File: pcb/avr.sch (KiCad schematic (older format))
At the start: 30 parts, among them IC2 ATMEGA168-P, P10 CONNECTOR, P11 CONNECTOR, P12 CONNECTOR, P13 CONNECTOR, P14 CONNECTOR, P15 CONNECTOR, P16 CONNECTOR, P17 CONNECTOR, P18 CONNECTOR, P19 CONNECTOR, P20 CONNECTOR, P21 CONNECTOR, P22 CONNECTOR, P23 CONNECTOR, P24 CONNECTOR, P25 CONN_01X03, P4 CONNECTOR, P5 CONNECTOR, P6 CONNECTOR, P7 CONNECTOR, P8 CONNECTOR, P9 CONNECTOR, x2 xtal_osc

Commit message: changed LED and boost converters Diode footprints. renumbered components
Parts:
- renumbered C13 to C201, C14 to C202, C10 to C203, C11 to C204, C12 to C205, IC2 to IC201, P4 to P201, P5 to P202, P6 to P203, P7 to P204, P8 to P205, P9 to P206, P10 to P207, P11 to P208, P12 to P209, P13 to P210, P14 to P211, P15 to P212, P16 to P213, P17 to P214, P18 to P215, P19 to P216, P20 to P217, P21 to P218, P22 to P219, P23 to P220, P24 to P221, P25 to P222, R5 to R201, x2 to x201
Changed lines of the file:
@@
 Connection ~ 4750 2900
 $Comp
-L xtal_osc x2
+L xtal_osc x201
 U 1 1 58B9F491
 P 8900 4000
-F 0 "x2" H 8750 4250 60  0000 C CNN
+F 0 "x201" H 8750 4250 60  0000 C CNN
 F 1 "xtal_osc" H 8900 4150 60  0000 C CNN
 F 2 "netl:SM_3225" H 8900 4050 60  0001 C CNN
@@
 $EndComp
 $Comp
-L GND #PWR015
+L GND #PWR202
 U 1 1 58B9F648
 P 4800 4950
-F 0 "#PWR015" H 4800 4700 50  0001 C CNN
+F 0 "#PWR202" H 4800 4700 50  0001 C CNN
 F 1 "GND" H 4800 4800 50  0000 C CNN
 F 2 "" H 4800 4950 50  0000 C CNN
@@
 Connection ~ 4800 4900
 $Comp
-L GND #PWR016
+L GND #PWR204
 U 1 1 58B9F675
 P 8900 4300
-F 0 "#PWR016" H 8900 4050 50  0001 C CNN
+F 0 "#PWR204" H 8900 4050 50  0001 C CNN
 F 1 "GND" H 8900 4150 50  0000 C CNN
 F 2 "" H 8900 4300 50  0000 C CNN
@@
 Connection ~ 8900 4300
 $Comp
-L C C10
+L C C203
 U 1 1 58B9F6BE
 P 8450 4150
-F 0 "C10" H 8475 4250 50  0000 L CNN
+F 0 "C203" H 8475 4250 50  0000 L CNN
 F 1 "C" H 8475 4050 50  0000 L CNN
 F 2 "netl:SMD_0603" H 8488 4000 50  0001 C CNN
@@
 $EndComp
 $Comp
-L C C12
+L C C205
 U 1 1 58B9F6FA
 P 9350 4150
-F 0 "C12" H 9375 4250 50  0000 L CNN
+F 0 "C205" H 9375 4250 50  0000 L CNN
 F 1 "C" H 9375 4050 50  0000 L CNN
 F 2 "netl:SMD_0603" H 9388 4000 50  0001 C CNN
@@
 $EndComp
 $Comp
-L GND #PWR017
+L GND #PWR203
 U 1 1 58B9F75B
 P 8450 4300
-F 0 "#PWR017" H 8450 4050 50  0001 C CNN
+F 0 "#PWR203" H 8450 4050 50  0001 C CNN
 F 1 "GND" H 8450 4150 50  0000 C CNN
 F 2 "" H 8450 4300 50  0000 C CNN
@@
 $EndComp
 $Comp
-L GND #PWR018
+L GND #PWR205
 U 1 1 58B9F772
 P 9350 4300
-F 0 "#PWR018" H 9350 4050 50  0001 C CNN
+F 0 "#PWR205" H 9350 4050 50  0001 C CNN
 F 1 "GND" H 9350 4150 50  0000 C CNN
 F 2 "" H 9350 4300 50  0000 C CNN
@@
 Connection ~ 9350 4000
 $Comp
-L R R5
+L R R201
 U 1 1 58B9FA6E
 P 9050 2900
-F 0 "R5" V 9130 2900 50  0000 C CNN
+F 0 "R201" V 9130 2900 50  0000 C CNN
 F 1 "R" V 9050 2900 50  0000 C CNN
 F 2 "netl:SMD_0603" V 8980 2900 50  0001 C CNN
@@
 ~DTR
 $Comp
-L C C11
+L C C204
 U 1 1 58B9FE16
 P 8900 3050
-F 0 "C11" H 8925 3150 50  0000 L CNN
+F 0 "C204" H 8925 3150 50  0000 L CNN
 F 1 "C" H 8925 2950 50  0000 L CNN
 F 2 "netl:SMD_0603" H 8938 2900 50  0001 C CNN
@@
 TX
 $Comp
-L C C13
+L C C201
 U 1 1 58BA2D1E
 P 4150 3000
-F 0 "C13" H 4175 3100 50  0000 L CNN
+F 0 "C201" H 4175 3100 50  0000 L CNN
 F 1 "C" H 4175 2900 50  0000 L CNN
 F 2 "netl:SMD_0603" H 4188 2850 50  0001 C CNN
@@
 $EndComp
 $Comp
-L C C14
+L C C202
 U 1 1 58BA4005
 P 4450 3000
-F 0 "C14" H 4475 3100 50  0000 L CNN
+F 0 "C202" H 4475 3100 50  0000 L CNN
 F 1 "C" H 4475 2900 50  0000 L CNN
 F 2 "netl:SMD_0603" H 4488 2850 50  0001 C CNN
@@
 $EndComp
 $Comp
-L GND #PWR019
+L GND #PWR201
 U 1 1 58BA4083
 P 4300 3250
-F 0 "#PWR019" H 4300 3000 50  0001 C CNN
+F 0 "#PWR201" H 4300 3000 50  0001 C CNN
 F 1 "GND" H 4300 3100 50  0000 C CNN
 F 2 "" H 4300 3250 50  0000 C CNN
@@
 Connection ~ 4300 2850
 $Comp
-L CONNECTOR P17
+L CONNECTOR P214
 U 1 1 58BA814A
 P 6850 4200
-F 0 "P17" H 7300 4200 70  0000 C CNN
+F 0 "P214" H 7300 4200 70  0000 C CNN
 F 1 "CONNECTOR" H 7150 4450 70  0001 C CNN
 F 2 "netl:1Pin_small" H 6850 4200 60  0001 C CNN
@@
 $EndComp
 $Comp
-L CONNECTOR P18
+L CONNECTOR P215
 U 1 1 58BA8D9B
 P 6850 4300
-F 0 "P18" H 7300 4300 70  0000 C CNN
+F 0 "P215" H 7300 4300 70  0000 C CNN
 F 1 "CONNECTOR" H 7150 4550 70  0001 C CNN
 F 2 "netl:1Pin_small" H 6850 4300 60  0001 C CNN
@@
 $EndComp
 $Comp
-L CONNECTOR P19
+L CONNECTOR P216
 U 1 1 58BA8DC9
 P 6850 4400
-F 0 "P19" H 7300 4400 70  0000 C CNN
+F 0 "P216" H 7300 4400 70  0000 C CNN
 F 1 "CONNECTOR" H 7150 4650 70  0001 C CNN
 F 2 "netl:1Pin_small" H 6850 4400 60  0001 C CNN
@@
 $EndComp
 $Comp
-L CONNECTOR P20
+L CONNECTOR P217
 U 1 1 58BA8DFA
 P 6850 4500
-F 0 "P20" H 7300 4500 70  0000 C CNN
+F 0 "P217" H 7300 4500 70  0000 C CNN
 F 1 "CONNECTOR" H 7150 4750 70  0001 C CNN
 F 2 "netl:1Pin_small" H 6850 4500 60  0001 C CNN
@@
 $EndComp
 $Comp
-L CONNECTOR P21
+L CONNECTOR P218
 U 1 1 58BA8E32
 P 6850 4600
-F 0 "P21" H 7300 4600 70  0000 C CNN
+F 0 "P218" H 7300 4600 70  0000 C CNN
 F 1 "CONNECTOR" H 7150 4850 70  0001 C CNN
 F 2 "netl:1Pin_small" H 6850 4600 60  0001 C CNN
@@
 $EndComp
 $Comp
-L CONNECTOR P22
+L CONNECTOR P219
 U 1 1 58BA8E6D
 P 6850 4700
-F 0 "P22" H 7300 4700 70  0000 C CNN
+F 0 "P219" H 7300 4700 70  0000 C CNN
 F 1 "CONNECTOR" H 7150 4950 70  0001 C CNN
 F 2 "netl:1Pin_small" H 6850 4700 60  0001 C CNN
@@
 $EndComp
 $Comp
-L CONNECTOR P23
+L CONNECTOR P220
 U 1 1 58BA8ED1
 P 6850 4800
-F 0 "P23" H 7300 4800 70  0000 C CNN
+F 0 "P220" H 7300 4800 70  0000 C CNN
 F 1 "CONNECTOR" H 7150 5050 70  0001 C CNN
 F 2 "netl:1Pin_small" H 6850 4800 60  0001 C CNN
@@
 $EndComp
 $Comp
-L CONNECTOR P24
+L CONNECTOR P221
 U 1 1 58BA8F12
 P 6850 4900
-F 0 "P24" H 7300 4900 70  0000 C CNN
+F 0 "P221" H 7300 4900 70  0000 C CNN
 F 1 "CONNECTOR" H 7150 5150 70  0001 C CNN
 F 2 "netl:1Pin_small" H 6850 4900 60  0001 C CNN
@@
 	6700 3450 6850 3450
 $Comp
-L CONNECTOR P10
+L CONNECTOR P207
 U 1 1 58BA94D6
 P 6850 3450
-F 0 "P10" H 7300 3450 70  0000 C CNN
+F 0 "P207" H 7300 3450 70  0000 C CNN
 F 1 "CONNECTOR" H 7150 3700 70  0001 C CNN
 F 2 "netl:1Pin_small" H 6850 3450 60  0001 C CNN
@@
 $EndComp
 $Comp
-L CONNECTOR P11
+L CONNECTOR P208
 U 1 1 58BA94DC
 P 6850 3550
-F 0 "P11" H 7300 3550 70  0000 C CNN
+F 0 "P208" H 7300 3550 70  0000 C CNN
 F 1 "CONNECTOR" H 7150 3800 70  0001 C CNN
 F 2 "netl:1Pin_small" H 6850 3550 60  0001 C CNN
@@
 $EndComp
 $Comp
-L CONNECTOR P12
+L CONNECTOR P209
 U 1 1 58BA94E2
 P 6850 3650
-F 0 "P12" H 7300 3650 70  0000 C CNN
+F 0 "P209" H 7300 3650 70  0000 C CNN
 F 1 "CONNECTOR" H 7150 3900 70  0001 C CNN
 F 2 "netl:1Pin_small" H 6850 3650 60  0001 C CNN
@@
 $EndComp
 $Comp
-L CONNECTOR P13
+L CONNECTOR P210
 U 1 1 58BA94E8
 P 6850 3750
-F 0 "P13" H 7300 3750 70  0000 C CNN
+F 0 "P210" H 7300 3750 70  0000 C CNN
 F 1 "CONNECTOR" H 7150 4000 70  0001 C CNN
 F 2 "netl:1Pin_small" H 6850 3750 60  0001 C CNN
@@
 $EndComp
 $Comp
-L CONNECTOR P14
+L CONNECTOR P211
 U 1 1 58BA94EE
 P 6850 3850
-F 0 "P14" H 7300 3850 70  0000 C CNN
+F 0 "P211" H 7300 3850 70  0000 C CNN
 F 1 "CONNECTOR" H 7150 4100 70  0001 C CNN
 F 2 "netl:1Pin_small" H 6850 3850 60  0001 C CNN
@@
 $EndComp
 $Comp
-L CONNECTOR P15
+L CONNECTOR P212
 U 1 1 58BA94F4
 P 6850 3950
-F 0 "P15" H 7300 3950 70  0000 C CNN
+F 0 "P212" H 7300 3950 70  0000 C CNN
 F 1 "CONNECTOR" H 7150 4200 70  0001 C CNN
 F 2 "netl:1Pin_small" H 6850 3950 60  0001 C CNN
@@
 $EndComp
 $Comp
-L CONNECTOR P16
+L CONNECTOR P213
 U 1 1 58BA94FA
 P 6850 4050
-F 0 "P16" H 7300 4050 70  0000 C CNN
+F 0 "P213" H 7300 4050 70  0000 C CNN
 F 1 "CONNECTOR" H 7150 4300 70  0001 C CNN
 F 2 "netl:1Pin_small" H 6850 4050 60  0001 C CNN
@@
 	6850 4050 6700 4050
 $Comp
-L ATMEGA168-P IC2
+L ATMEGA168-P IC201
 U 1 1 58B9E598
 P 5800 3750
-F 0 "IC2" H 4950 5050 50  0000 L BNN
+F 0 "IC201" H 4950 5050 50  0000 L BNN
 F 1 "ATMEGA168-P" H 6150 2400 50  0000 L BNN
 F 2 "Housings_QFP:TQFP-32_7x7mm_Pitch0.8mm" H 5800 2350 50  0000 C CIN
@@
 $EndComp
 Wire Wire Line
-	6700 4200 6850 4200
-Wire Wire Line
-	6850 4300 6700 4300
-Wire Wire Line
-	6700 4300 6700 4250
-Wire Wire Line
-	6700 4150 6700 4200
-Wire Wire Line
 	6700 2600 6850 2600
 $Comp
-L CONNECTOR P4
+L CONNECTOR P201
 U 1 1 58BA9F9A
 P 6850 2600
-F 0 "P4" H 7300 2600 70  0000 C CNN
+F 0 "P201" H 7300 2600 70  0000 C CNN
 F 1 "CONNECTOR" H 7150 2850 70  0001 C CNN
 F 2 "netl:1Pin_small" H 6850 2600 60  0001 C CNN
@@
 $EndComp
 $Comp
-L CONNECTOR P5
+L CONNECTOR P202
 U 1 1 58BA9FA0
 P 6850 2700
-F 0 "P5" H 7300 2700 70  0000 C CNN
+F 0 "P202" H 7300 2700 70  0000 C CNN
 F 1 "CONNECTOR" H 7150 2950 70  0001 C CNN
 F 2 "netl:1Pin_small" H 6850 2700 60  0001 C CNN
@@
 $EndComp
 $Comp
-L CONNECTOR P6
+L CONNECTOR P203
 U 1 1 58BA9FA6
 P 6850 2800
-F 0 "P6" H 7300 2800 70  0000 C CNN
+F 0 "P203" H 7300 2800 70  0000 C CNN
 F 1 "CONNECTOR" H 7150 3050 70  0001 C CNN
 F 2 "netl:1Pin_small" H 6850 2800 60  0001 C CNN
@@
 $EndComp
 $Comp
-L CONNECTOR P7
+L CONNECTOR P204
 U 1 1 58BA9FAC
 P 6850 2900
-F 0 "P7" H 7300 2900 70  0000 C CNN
+F 0 "P204" H 7300 2900 70  0000 C CNN
 F 1 "CONNECTOR" H 7150 3150 70  0001 C CNN
 F 2 "netl:1Pin_small" H 6850 2900 60  0001 C CNN
@@
 $EndComp
 $Comp
-L CONNECTOR P8
+L CONNECTOR P205
 U 1 1 58BA9FB2
 P 6850 3000
-F 0 "P8" H 7300 3000 70  0000 C CNN
+F 0 "P205" H 7300 3000 70  0000 C CNN
 F 1 "CONNECTOR" H 7150 3250 70  0001 C CNN
 F 2 "netl:1Pin_small" H 6850 3000 60  0001 C CNN
@@
 $EndComp
 $Comp
-L CONNECTOR P9
+L CONNECTOR P206
 U 1 1 58BA9FB8
 P 6850 3100
-F 0 "P9" H 7300 3100 70  0000 C CNN
+F 0 "P206" H 7300 3100 70  0000 C CNN
 F 1 "CONNECTOR" H 7150 3350 70  0001 C CNN
 F 2 "netl:1Pin_small" H 6850 3100 60  0001 C CNN
@@
 	6700 3100 6850 3100
 $Comp
-L CONN_01X03 P25
+L CONN_01X03 P222
 U 1 1 58BAB28B
 P 10600 4200
-F 0 "P25" H 10600 4400 50  0000 C CNN
+F 0 "P222" H 10600 4400 50  0000 C CNN
 F 1 "CONN_01X03" V 10700 4200 50  0000 C CNN
 F 2 "netl:SM_3_WIRE" H 10600 4200 50  0000 C CNN
@@
 $EndComp
 $Comp
-L GND #PWR020
+L GND #PWR206
 U 1 1 58BAB3DE
 P 10350 4350
-F 0 "#PWR020" H 10350 4100 50  0001 C CNN
+F 0 "#PWR206" H 10350 4100 50  0001 C CNN
 F 1 "GND" H 10350 4200 50  0000 C CNN
 F 2 "" H 10350 4350 50  0000 C CNN
@@
 Wire Wire Line
 	10400 4100 10350 4100
+Wire Wire Line
+	6700 4200 6850 4200
+Wire Wire Line
+	6700 4150 6700 4200
+Wire Wire Line
+	6700 4300 6850 4300
+Wire Wire Line
+	6700 4250 6700 4300
 $EndSCHEMATC

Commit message: changed mcu to the correct one. redid layout
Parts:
- removed IC201: ATMEGA168-P, Housings_QFP:TQFP-32_7x7mm_Pitch0.8mm, symbol ATMEGA168-P
- added IC201: ATMEGA328P-M, MLF/QFN32, symbol ATMEGA328P-M
- added P223, P224: CONNECTOR, netl:1Pin_small, symbol CONNECTOR
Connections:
- wire segments 43 -> 44
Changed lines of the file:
@@
 	4650 4900 4800 4900
 Wire Wire Line
-	4800 4800 4800 4950
+	4800 4700 4800 4950
 Text HLabel 4350 2600 0    60   Input ~ 0
 VCC
@@
 $EndComp
 $Comp
-L GND #PWR202
+L GND #PWR08
 U 1 1 58B9F648
 P 4800 4950
-F 0 "#PWR202" H 4800 4700 50  0001 C CNN
+F 0 "#PWR08" H 4800 4700 50  0001 C CNN
 F 1 "GND" H 4800 4800 50  0000 C CNN
 F 2 "" H 4800 4950 50  0000 C CNN
@@
 Connection ~ 4800 4900
 $Comp
-L GND #PWR204
+L GND #PWR09
 U 1 1 58B9F675
 P 8900 4300
-F 0 "#PWR204" H 8900 4050 50  0001 C CNN
+F 0 "#PWR09" H 8900 4050 50  0001 C CNN
 F 1 "GND" H 8900 4150 50  0000 C CNN
 F 2 "" H 8900 4300 50  0000 C CNN
@@
 $EndComp
 $Comp
-L GND #PWR203
+L GND #PWR010
 U 1 1 58B9F75B
 P 8450 4300
-F 0 "#PWR203" H 8450 4050 50  0001 C CNN
+F 0 "#PWR010" H 8450 4050 50  0001 C CNN
 F 1 "GND" H 8450 4150 50  0000 C CNN
 F 2 "" H 8450 4300 50  0000 C CNN
@@
 $EndComp
 $Comp
-L GND #PWR205
+L GND #PWR011
 U 1 1 58B9F772
 P 9350 4300
-F 0 "#PWR205" H 9350 4050 50  0001 C CNN
+F 0 "#PWR011" H 9350 4050 50  0001 C CNN
 F 1 "GND" H 9350 4150 50  0000 C CNN
 F 2 "" H 9350 4300 50  0000 C CNN
@@
 $EndComp
 $Comp
-L GND #PWR201
+L GND #PWR012
 U 1 1 58BA4083
 P 4300 3250
-F 0 "#PWR201" H 4300 3000 50  0001 C CNN
+F 0 "#PWR012" H 4300 3000 50  0001 C CNN
 F 1 "GND" H 4300 3100 50  0000 C CNN
 F 2 "" H 4300 3250 50  0000 C CNN
@@
 	6850 4050 6700 4050
 $Comp
-L ATMEGA168-P IC201
-U 1 1 58B9E598
-P 5800 3750
-F 0 "IC201" H 4950 5050 50  0000 L BNN
-F 1 "ATMEGA168-P" H 6150 2400 50  0000 L BNN
-F 2 "Housings_QFP:TQFP-32_7x7mm_Pitch0.8mm" H 5800 2350 50  0000 C CIN
-F 3 "" H 5800 3750 50  0000 C CNN
-	1    5800 3750
-	1    0    0    -1
-$EndComp
-Wire Wire Line
-	6700 2600 6850 2600
-$Comp
 L CONNECTOR P201
 U 1 1 58BA9F9A
@@
 $EndComp
 $Comp
-L GND #PWR206
+L GND #PWR013
 U 1 1 58BAB3DE
 P 10350 4350
-F 0 "#PWR206" H 10350 4100 50  0001 C CNN
+F 0 "#PWR013" H 10350 4100 50  0001 C CNN
 F 1 "GND" H 10350 4200 50  0000 C CNN
 F 2 "" H 10350 4350 50  0000 C CNN
@@
 Wire Wire Line
 	10350 4300 10350 4350
-Text Label 6700 2600 0    60   ~ 0
+Text Label 6700 4400 0    60   ~ 0
 LED_SRIP
 Text Label 10350 4200 2    60   ~ 0
@@
 Wire Wire Line
 	6700 4250 6700 4300
+$Comp
+L ATMEGA328P-M IC201
+U 1 1 590DDCB6
+P 5700 3700
+F 0 "IC201" H 4950 4950 50  0000 L BNN
+F 1 "ATMEGA328P-M" H 6100 2300 50  0000 L BNN
+F 2 "MLF/QFN32" H 5700 3700 50  0000 C CIN
+F 3 "" H 5700 3700 50  0000 C CNN
+	1    5700 3700
+	1    0    0    -1
+$EndComp
+Wire Wire Line
+	4800 2700 4750 2700
+Connection ~ 4750 2700
+Connection ~ 4800 4800
+$Comp
+L CONNECTOR P223
+U 1 1 590DE73E
+P 4800 3950
+F 0 "P223" H 5250 3950 70  0000 C CNN
+F 1 "CONNECTOR" H 5100 4200 70  0001 C CNN
+F 2 "netl:1Pin_small" H 4800 3950 60  0001 C CNN
+F 3 "" H 4800 3950 60  0000 C CNN
+	1    4800 3950
+	-1   0    0    1
+$EndComp
+$Comp
+L CONNECTOR P224
+U 1 1 590DEA2E
+P 4800 4050
+F 0 "P224" H 5250 4050 70  0000 C CNN
+F 1 "CONNECTOR" H 5100 4300 70  0001 C CNN
+F 2 "netl:1Pin_small" H 4800 4050 60  0001 C CNN
+F 3 "" H 4800 4050 60  0000 C CNN
+	1    4800 4050
+	-1   0    0    1
+$EndComp
+Wire Wire Line
+	6850 2600 6700 2600
 $EndSCHEMATC

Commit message: updated component values
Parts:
- C201, C202, C204: value C -> 100n
- C203, C205: value C -> 22p
- R201: value R -> 10k
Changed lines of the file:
@@
 P 8450 4150
 F 0 "C203" H 8475 4250 50  0000 L CNN
-F 1 "C" H 8475 4050 50  0000 L CNN
+F 1 "22p" H 8475 4050 50  0000 L CNN
 F 2 "netl:SMD_0603" H 8488 4000 50  0001 C CNN
 F 3 "" H 8450 4150 50  0000 C CNN
@@
 P 9350 4150
 F 0 "C205" H 9375 4250 50  0000 L CNN
-F 1 "C" H 9375 4050 50  0000 L CNN
+F 1 "22p" H 9375 4050 50  0000 L CNN
 F 2 "netl:SMD_0603" H 9388 4000 50  0001 C CNN
 F 3 "" H 9350 4150 50  0000 C CNN
@@
 P 9050 2900
 F 0 "R201" V 9130 2900 50  0000 C CNN
-F 1 "R" V 9050 2900 50  0000 C CNN
+F 1 "10k" V 9050 2900 50  0000 C CNN
 F 2 "netl:SMD_0603" V 8980 2900 50  0001 C CNN
 F 3 "" H 9050 2900 50  0000 C CNN
@@
 P 8900 3050
 F 0 "C204" H 8925 3150 50  0000 L CNN
-F 1 "C" H 8925 2950 50  0000 L CNN
+F 1 "100n" H 8925 2950 50  0000 L CNN
 F 2 "netl:SMD_0603" H 8938 2900 50  0001 C CNN
 F 3 "" H 8900 3050 50  0000 C CNN
@@
 P 4150 3000
 F 0 "C201" H 4175 3100 50  0000 L CNN
-F 1 "C" H 4175 2900 50  0000 L CNN
+F 1 "100n" H 4175 2900 50  0000 L CNN
 F 2 "netl:SMD_0603" H 4188 2850 50  0001 C CNN
 F 3 "" H 4150 3000 50  0000 C CNN
@@
 P 4450 3000
 F 0 "C202" H 4475 3100 50  0000 L CNN
-F 1 "C" H 4475 2900 50  0000 L CNN
+F 1 "100n" H 4475 2900 50  0000 L CNN
 F 2 "netl:SMD_0603" H 4488 2850 50  0001 C CNN
 F 3 "" H 4450 3000 50  0000 C CNN

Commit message: centered battery tab connectors, reworked layout to match it
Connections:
- net LED_SRIP: now also IC201.1 ((PCINT19/OC2B/INT1)PD3), P217.1 (W); no longer IC201.32 ((PCINT18/INT0)PD2), P216.1 (W)
- new net BTN: IC201.32 ((PCINT18/INT0)PD2), P216.1 (W)
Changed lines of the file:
@@
 Wire Wire Line
 	10350 4300 10350 4350
-Text Label 6700 4400 0    60   ~ 0
+Text Label 6700 4500 0    60   ~ 0
 LED_SRIP
 Text Label 10350 4200 2    60   ~ 0
@@
 Wire Wire Line
 	6850 2600 6700 2600
+Text Label 6700 4400 0    60   ~ 0
+BTN
 $EndSCHEMATC

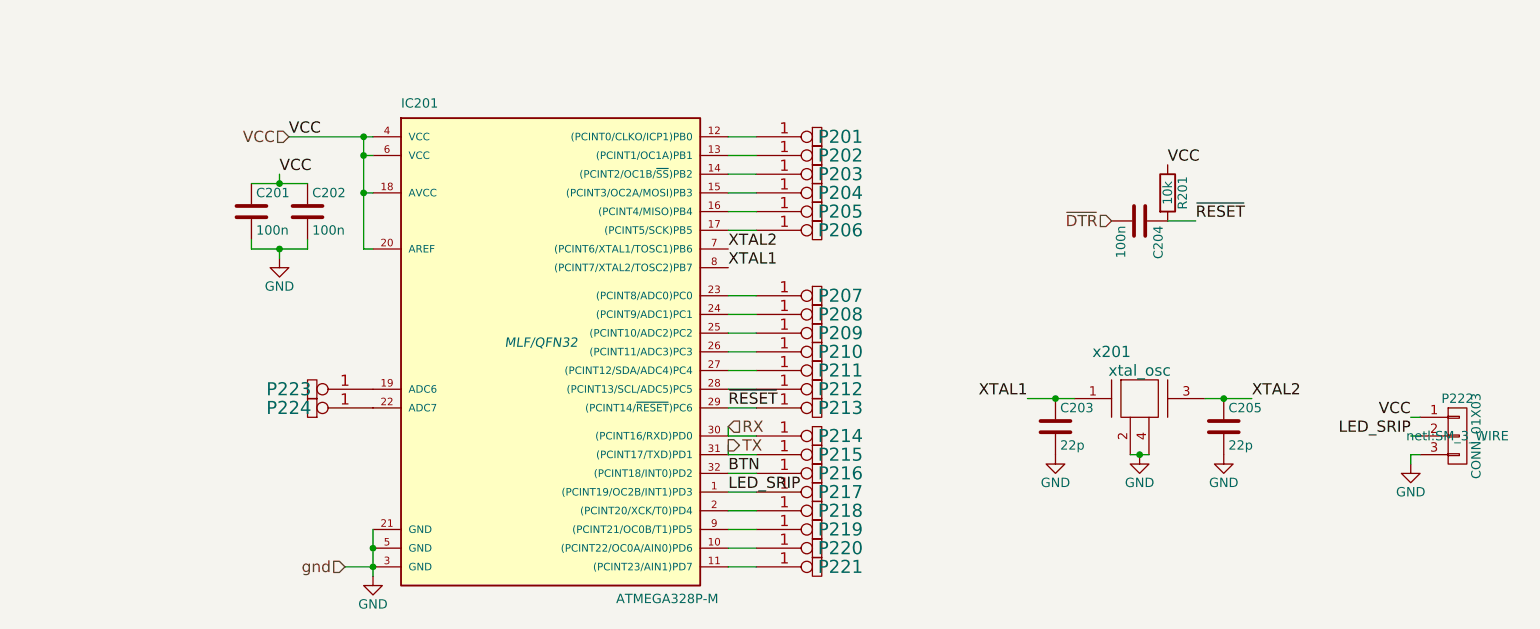
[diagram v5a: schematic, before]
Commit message: reworked bms and mcu to use seeed components
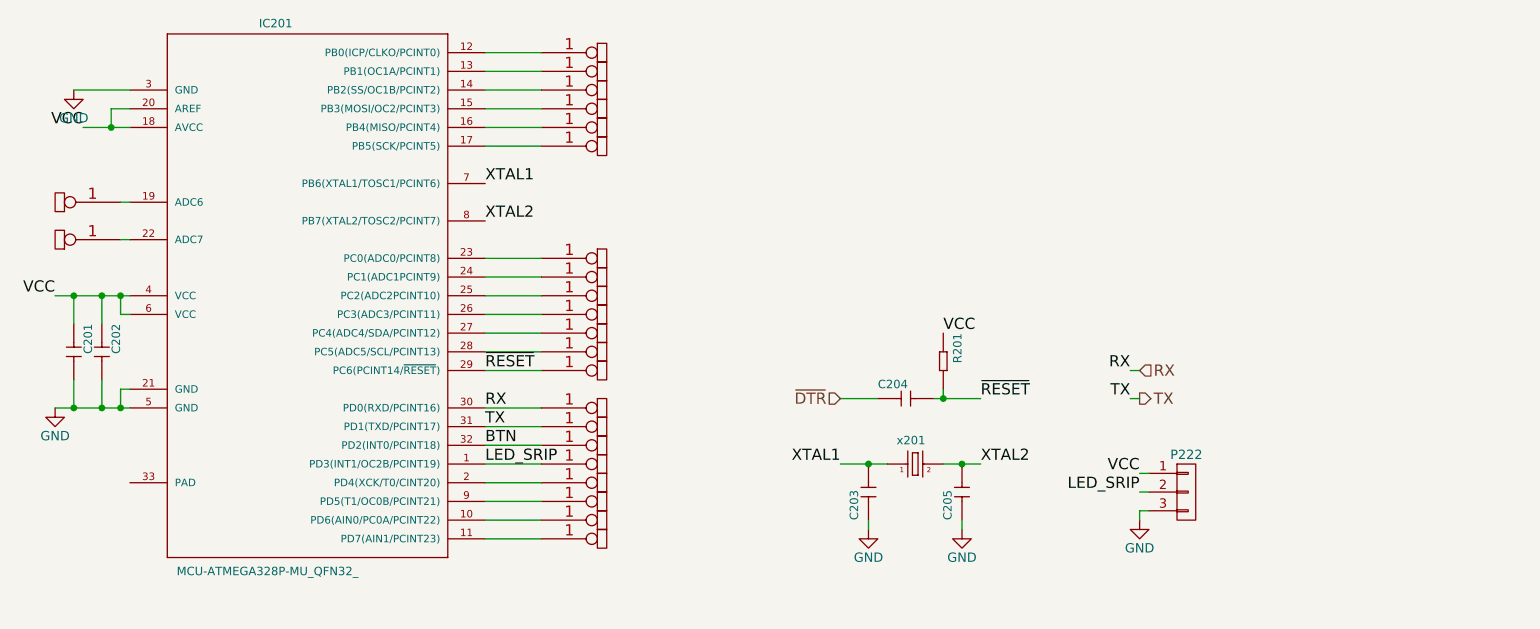
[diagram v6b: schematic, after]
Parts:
- removed C201, C202, C204: 100n, netl:SMD_0603, symbol C
- removed C203, C205: 22p, netl:SMD_0603, symbol C
- removed IC201: ATMEGA328P-M, MLF/QFN32, symbol ATMEGA328P-M
- removed R201: 10k, netl:SMD_0603, symbol R
- removed x201: xtal_osc, netl:SM_3225, symbol xtal_osc
- added C201, C202, C204: CERAMIC-100NF-50V-10%-X7R_0603_, SeeedOPL-Capacitor-2016:C0603, symbol CERAMIC-100NF-50V-10%-X7R_0603_
- added C203, C205: CERAMIC-22PF-50V-5%-NPO_0603_, SeeedOPL-Capacitor-2016:C0603, symbol CERAMIC-22PF-50V-5%-NPO_0603_
- added IC201: MCU-ATMEGA328P-MU_QFN32_, SeeedOPL-IC-2016:QFN32G-0.5-5X5MM, symbol MCU-ATMEGA328P-MU_QFN32_
- added R201: SMD-RES-10K-1%-1_10W_0603_, SeeedOPL-Resistor-2016:R0603, symbol SMD-RES-10K-1%-1_10W_0603_
- added x201: SMD-CRYSTAL-16MHZ-8PF-20PPM-40R_2P-5.0X3.2MM_, SeeedOPL-Crystal Oscillator-2016:X2-SMD-5.0X3.2X1.3MM, symbol SMD-CRYSTAL-16MHZ-8PF-20PPM-40R_2P-5.0X3.2MM_
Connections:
- net BTN: now also IC201.32 (PD2(INT0/PCINT18))
- net GND: now also C201.2, C202.2, C203.1, C205.1, IC201.21 (GND), IC201.3 (GND), IC201.5 (GND)
- net LED_SRIP: now also IC201.1 (PD3(INT1/OC2B/PCINT19))
- net RX: now also IC201.30 (PD0(RXD/PCINT16))
- net TX: now also IC201.31 (PD1(TXD/PCINT17))
- net VCC: now also C201.1, C202.1, IC201.18 (AVCC), IC201.20 (AREF), IC201.4 (VCC), IC201.6 (VCC), R201.1
- net XTAL1: now also C203.2, IC201.7 (PB6(XTAL1/TOSC1/PCINT6)), x201.1
- net XTAL2: now also C205.2, IC201.8 (PB7(XTAL2/TOSC2/PCINT7)), x201.2
- net ~DTR: now also C204.1
- net ~RESET: now also C204.2, IC201.29 (PC6(PCINT14/~RESET)), R201.2
- net at P218.1 (W): now also IC201.2 (PD4(XCK/T0/CINT20))
- net at P219.1 (W): now also IC201.9 (PD5(T1/OC0B/PCINT21))
- net at P220.1 (W): now also IC201.10 (PD6(AIN0/PC0A/PCINT22))
- net at P221.1 (W): now also IC201.11 (PD7(AIN1/PCINT23))
- net at P207.1 (W): now also IC201.23 (PC0(ADC0/PCINT8))
- net at P208.1 (W): now also IC201.24 (PC1(ADC1PCINT9))
- net at P209.1 (W): now also IC201.25 (PC2(ADC2PCINT10))
- net at P210.1 (W): now also IC201.26 (PC3(ADC3/PCINT11))
- net at P211.1 (W): now also IC201.27 (PC4(ADC4/SDA/PCINT12))
- net at P212.1 (W): now also IC201.28 (PC5(ADC5/SCL/PCINT13))
- net at P201.1 (W): now also IC201.12 (PB0(ICP/CLKO/PCINT0))
- net at P202.1 (W): now also IC201.13 (PB1(OC1A/PCINT1))
- net at P203.1 (W): now also IC201.14 (PB2(SS/OC1B/PCINT2))
- net at P204.1 (W): now also IC201.15 (PB3(MOSI/OC2/PCINT3))
- net at P205.1 (W): now also IC201.16 (PB4(MISO/PCINT4))
- net at P206.1 (W): now also IC201.17 (PB5(SCK/PCINT5))
- net at P223.1 (W): now also IC201.19 (ADC6)
- net at P224.1 (W): now also IC201.22 (ADC7)
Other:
- moved on the sheet: P222
